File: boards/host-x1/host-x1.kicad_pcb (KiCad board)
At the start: 4 copper layers, 91 x 83 mm, 232 parts, among them J1 CONN_3_PWROUT, J2 XILINX_JTAG, J3 STARSHIPRAIDER_IOBOARD_HOST, J4 BEL_FUSE_0826-1G1T-23-F, J5 PMOD_HEADER, J6 PMOD_HEADER, M1 LOGO_LONGTHING, M2 LOGO_ROHS, M3 LOGO_WEEE, M4 HOLE, M5 HOLE, M6 HOLE, M7 HOLE, Q1 SSM6N58NU, Q2 SSM6N58NU, Q3 SSM6N58NU, Q4 SSM6N58NU, SW1 SW_Push, U1 OLK-T_3-W12P-C, U10 DSC6102CI2A-100.0000, U11 S25FS064S_BGA, U2 XC7A100T-1FTG256C, U3 LTC3374-QFN, U4 S27KS0641DPBHI02, U5 S27KS0641DPBHI02, U6 S27KS0641DPBHI02, U7 S27KS0641DPBHI02, U8 KSZ9031RN, U9 DSC6101CI2A-025.0000

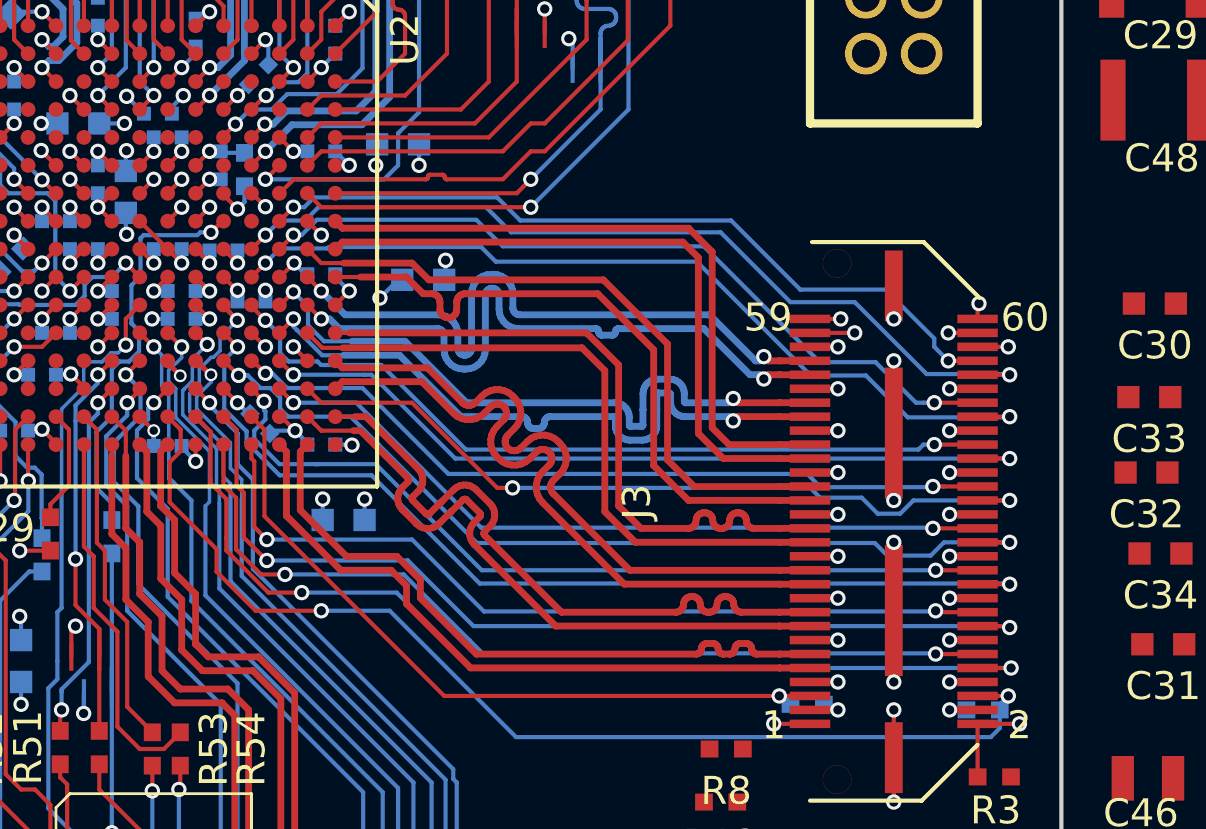
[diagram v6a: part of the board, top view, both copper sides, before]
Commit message: Length-matched I/O header
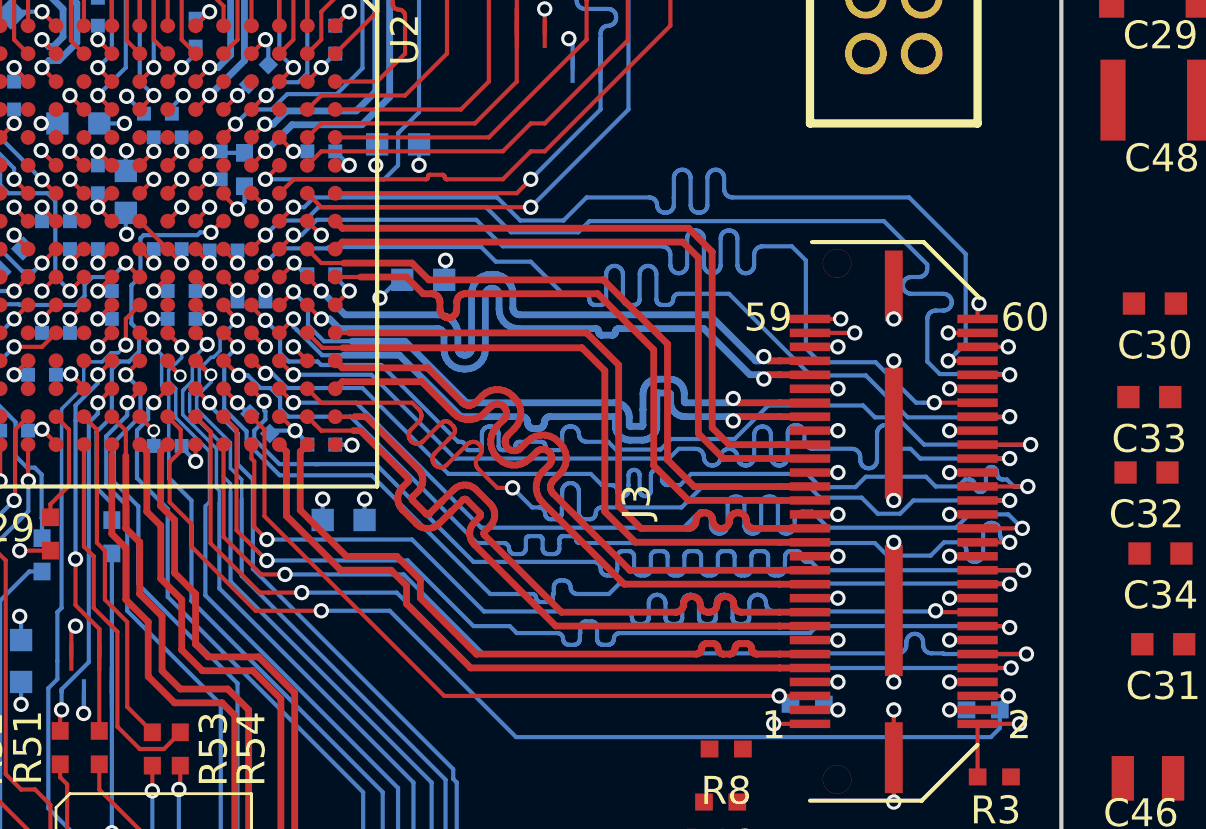
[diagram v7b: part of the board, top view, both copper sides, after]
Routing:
- net /Line Card/OE2: track 30.1 -> 41.4 mm
- net /Line Card/OE3: track 27.1 -> 36.5 mm
- net /Line Card/OE4: track 27.9 -> 36.5 mm
- net /Line Card/OE7: track 28.0 -> 36.5 mm
- net /Line Card/OE6: track 28.1 -> 36.5 mm
- net /Line Card/TXD4: track 28.4 -> 36.5 mm
- net /Line Card/OE5: track 28.6 -> 36.4 mm
- net /Line Card/TXD5: track 28.7 -> 36.4 mm
- net /Line Card/OE1: track 30.2 -> 36.5 mm
- net /Line Card/TXD6: track 31.3 -> 36.5 mm
- net /Line Card/TXD7: track 31.4 -> 36.5 mm
- net /Line Card/OE0: track 32.0 -> 36.4 mm
- net /Line Card/TXD3: track 32.6 -> 36.5 mm
- net /Line Card/TXD1: track 34.6 -> 36.6 mm
- net /Line Card/TXD2: track 35.2 -> 36.6 mm

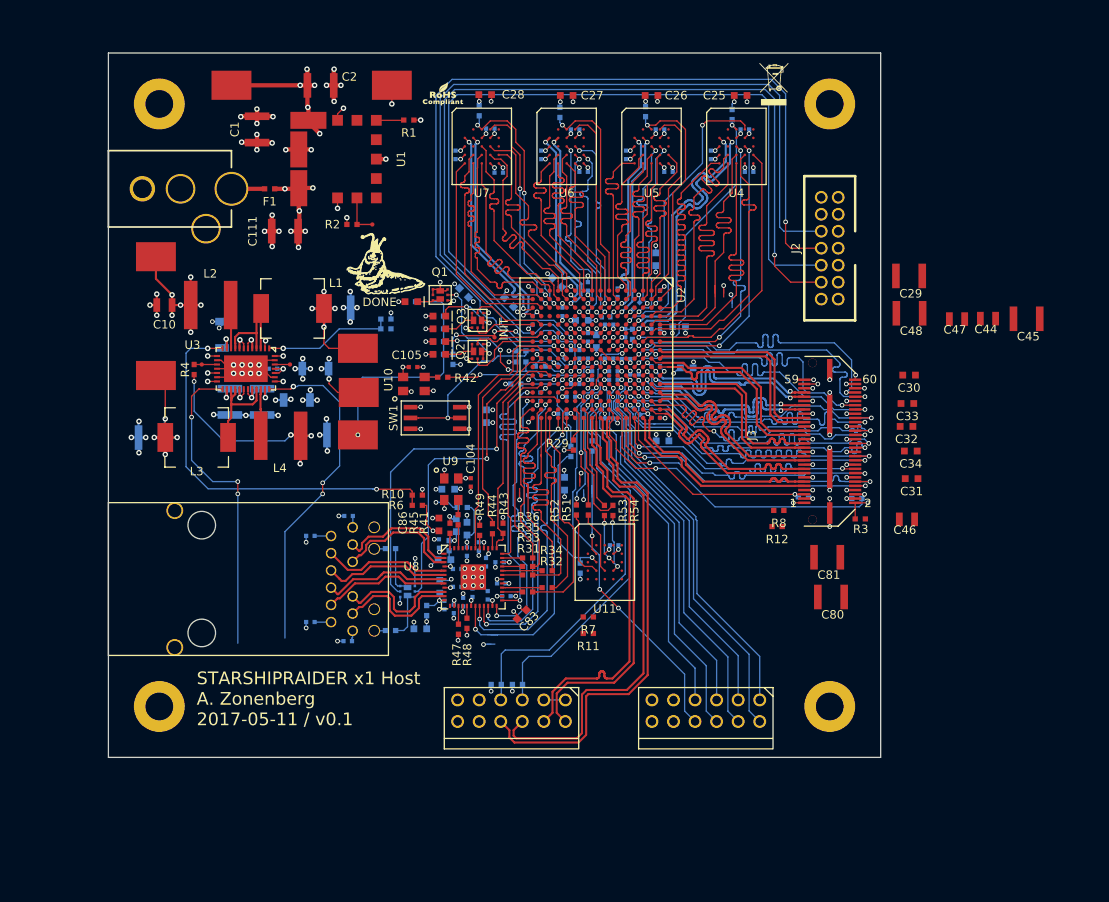
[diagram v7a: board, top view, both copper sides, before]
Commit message: Initial routing of remote sense
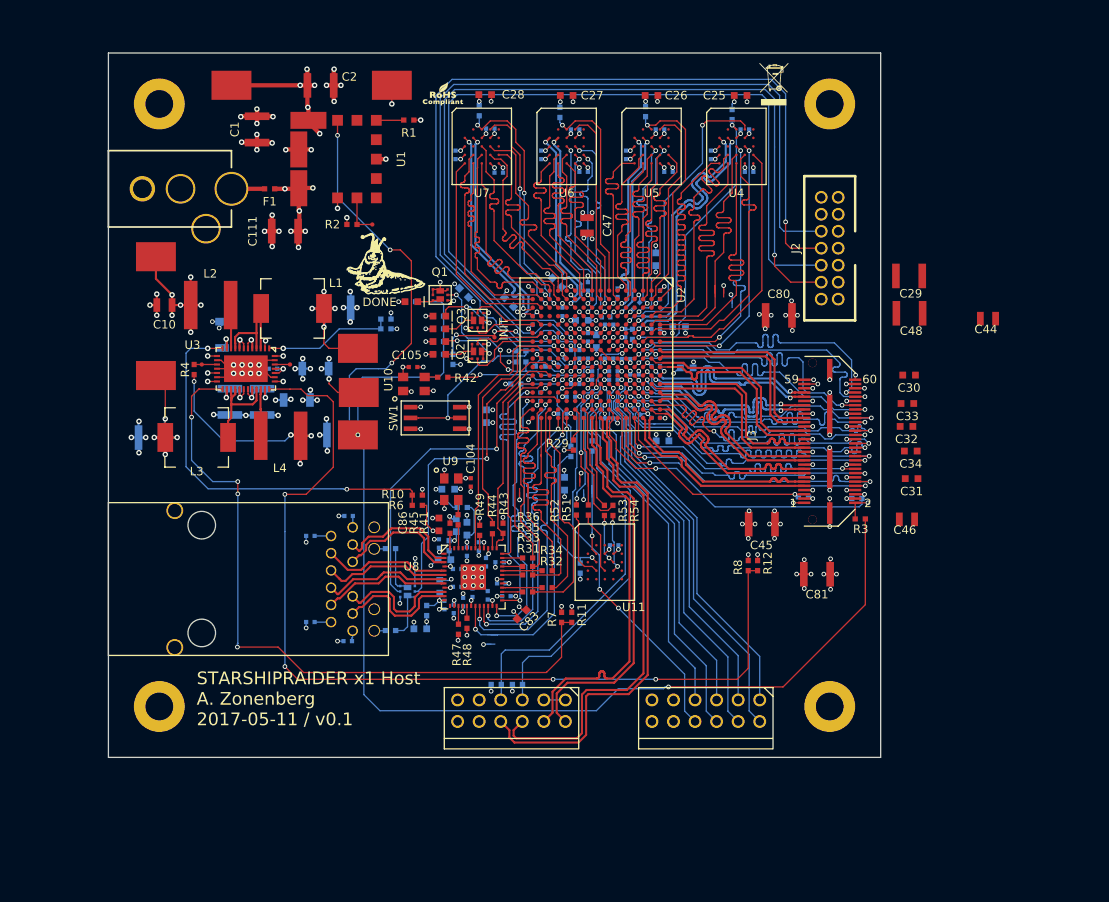
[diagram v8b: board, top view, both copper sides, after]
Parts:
- moved C47 45.0 mm to (85.4, 38.3), turned to 90 degrees
- moved C45 39.5 mm to (106.0, 73.5)
- moved C80 33.8 mm to (108.0, 48.9)
- moved R8 7.43 mm to (104.4, 78.4), turned to 90 degrees
- moved R12 5.14 mm to (105.5, 78.4), turned to 270 degrees
- moved R7 3.15 mm to (82.4, 84.5), turned to 90 degrees
- moved R11 2.72 mm to (83.6, 84.5), turned to 270 degrees
- moved C81 2.33 mm to (112.5, 79.4)
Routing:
- net /Power Supply/5V0_SENSE: track 1.74 -> 152.9 mm, vias 1 -> 4
- net /Power Supply/3V3_FB: track 39.8 -> 111.6 mm, vias 3 -> 4
- net /GND: track 1075.5 -> 1135.8 mm, vias 198 -> 214
- net /Power Supply/1V8_FB: track 37.1 -> 83.0 mm, vias 3 -> 4
- net /3V3: track 307.3 -> 333.8 mm, vias 20 -> 28
- net /5V0: track 238.5 -> 257.3 mm, vias 28 -> 32
- net /1V8: track 458.0 -> 474.5 mm, vias 66 -> 69
- net /1V0: track 92.8 -> 108.4 mm, vias 15 -> 16
- net /Flash / Ethernet/ETH_ACTIVITY_LED: track 41.7 -> 40.6 mm
